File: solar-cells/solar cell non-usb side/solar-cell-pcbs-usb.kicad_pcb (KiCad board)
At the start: 2 copper layers, 80 x 103.5 mm, 13 parts, among them J1 Solar Cell

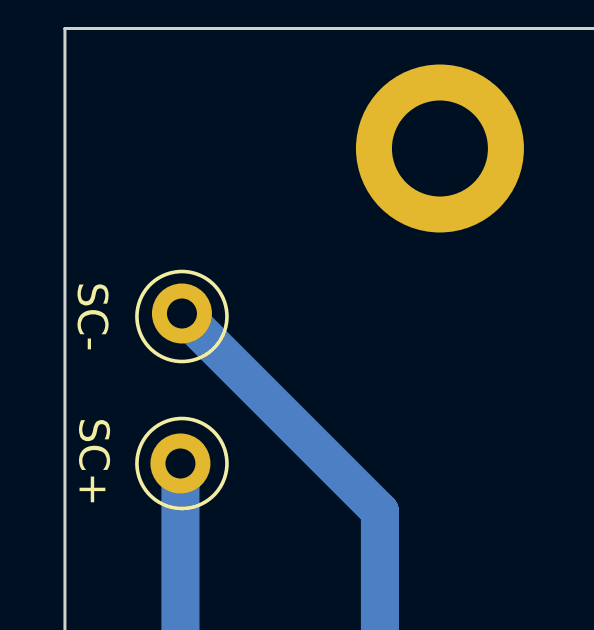
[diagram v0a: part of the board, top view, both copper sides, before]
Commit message: more annotations and connected test points
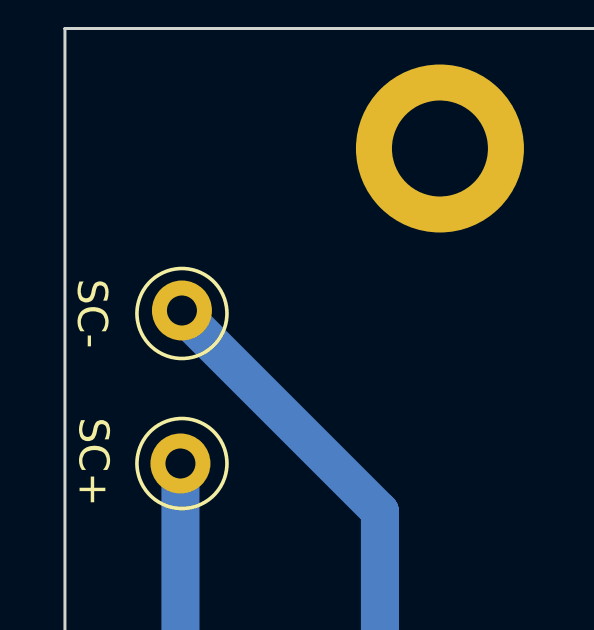
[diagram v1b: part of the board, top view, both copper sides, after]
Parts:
- moved TP2 0.10 mm to (76.0, 48.2)
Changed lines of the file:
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@@
   )
   (paper "A4")
+  (title_block
+    (title "Solar Cell PCB (non-USB side)")
+    (date "2022-12-25")
+    (rev "2")
+  )
   (layers
     (0 "F.Cu" signal)
@@
   )
   (footprint "TestPoint:TestPoint_Loop_D1.80mm_Drill1.0mm_Beaded" (layer "F.Cu")
-    (at 76 48.35)
+    (at 76 48.25)
     (descr "wire loop with bead as test point, loop diameter 1.8mm, hole diameter 1.0mm")
     (tags "test point wire loop bead")
@@
   )
   (dimension (type aligned) (layer "Dwgs.User")
+    (pts (xy 76 53.25) (xy 76 48.25))
+    (height -6.5)
+    (gr_text "5.0000 mm" (at 67.7 50.75 90) (layer "Dwgs.User")
+      (effects (font (size 1.5 1.5) (thickness 0.3)))
+    )
+    (format (units 3) (units_format 1) (precision 4))
+    (style (thickness 0.2) (arrow_length 1.27) (text_position_mode 0) (extension_height 0.58642) (extension_offset 0.5) keep_text_aligned)
+  )
+  (dimension (type aligned) (layer "Dwgs.User")
     (pts (xy 72.1 38.75) (xy 72.1 142.25))
     (height 17.849999)
@@
       (effects (font (size 1.5 1.5) (thickness 0.3)))
     )
+    (format (units 3) (units_format 1) (precision 4))
+    (style (thickness 0.2) (arrow_length 1.27) (text_position_mode 0) (extension_height 0.58642) (extension_offset 0.5) keep_text_aligned)
+  )
+  (dimension (type aligned) (layer "Dwgs.User")
+    (pts (xy 82.6 112.7) (xy 82.6 68.3))
+    (height -16.85)
+    (gr_text "44.4000 mm" (at 63.95 90.5 90) (layer "Dwgs.User")
+      (effects (font (size 1.5 1.5) (thickness 0.3)))
+    )
